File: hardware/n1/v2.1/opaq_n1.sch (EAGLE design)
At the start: 44 parts, among them IC1 RT9013-XXXB, IC2 TS5A3157, IC3 ATSHA204_SOIC8, IC4 ACS712, IC5 ADS1100, IC6 ATMega-328, IC7 AT25F512BWIDE_5.3MM, IC8 LM2594HV, K1 62101021021, Q1 IRLR3915, Q2 IRLR3915, Q3 IRLR3915, Q4 IRLR3915, X1 16 MHz

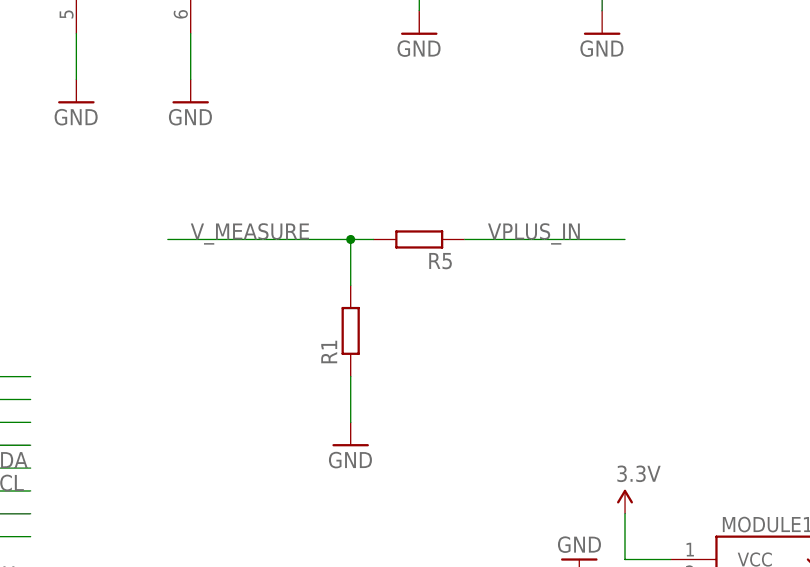
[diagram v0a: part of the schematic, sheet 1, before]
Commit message: Updated the Opaq n1 firmware to read the external temperature and the input voltage. Added the support for the external flash. Renamed the folder of the Opaq n1 hardware.
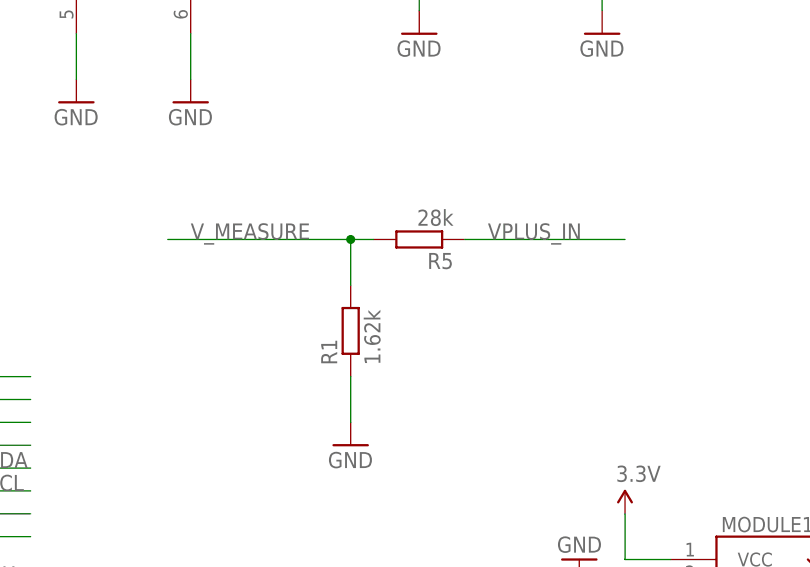
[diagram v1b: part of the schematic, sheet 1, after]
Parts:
- R1: value (none) -> 1.62k
- R5: value (none) -> 28k
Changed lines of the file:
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@@
 <part name="C7" library="SparkFun-Passives" deviceset="CAP" device="0402-CAP" value="100pf"/>
 <part name="FRAME2" library="SparkFun-Aesthetics" deviceset="FRAME-LETTER" device="NO_PACKAGE"/>
-<part name="R1" library="resistor" deviceset="R-EU_" device="R0805"/>
-<part name="R5" library="resistor" deviceset="R-EU_" device="R0805"/>
+<part name="R1" library="resistor" deviceset="R-EU_" device="R0805" value="1.62k"/>
+<part name="R5" library="resistor" deviceset="R-EU_" device="R0805" value="28k"/>
 <part name="GND13" library="supply1" deviceset="GND" device=""/>
 <part name="D1" library="SparkFun" deviceset="DIODE" device="SMA" value="SS36"/>
